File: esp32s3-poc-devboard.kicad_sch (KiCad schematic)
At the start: 69 parts, among them J1 24VDC, J2 Conn_01x01_Pin, J3 USB_C_Receptacle_USB2.0_14P, J4 USB_C_Receptacle_USB2.0_14P, Q3 MMDT5551, SW1 SW_Push, SW2 SW_Push, U1 ESP32-S3, U2 AMS1117-3.3, U3 XC6206P332MR, U4 TPS5430DDA, U5 CP2102N-A02-GQFN24, U6 USBLC6-2SC6, U7 USBLC6-2SC6

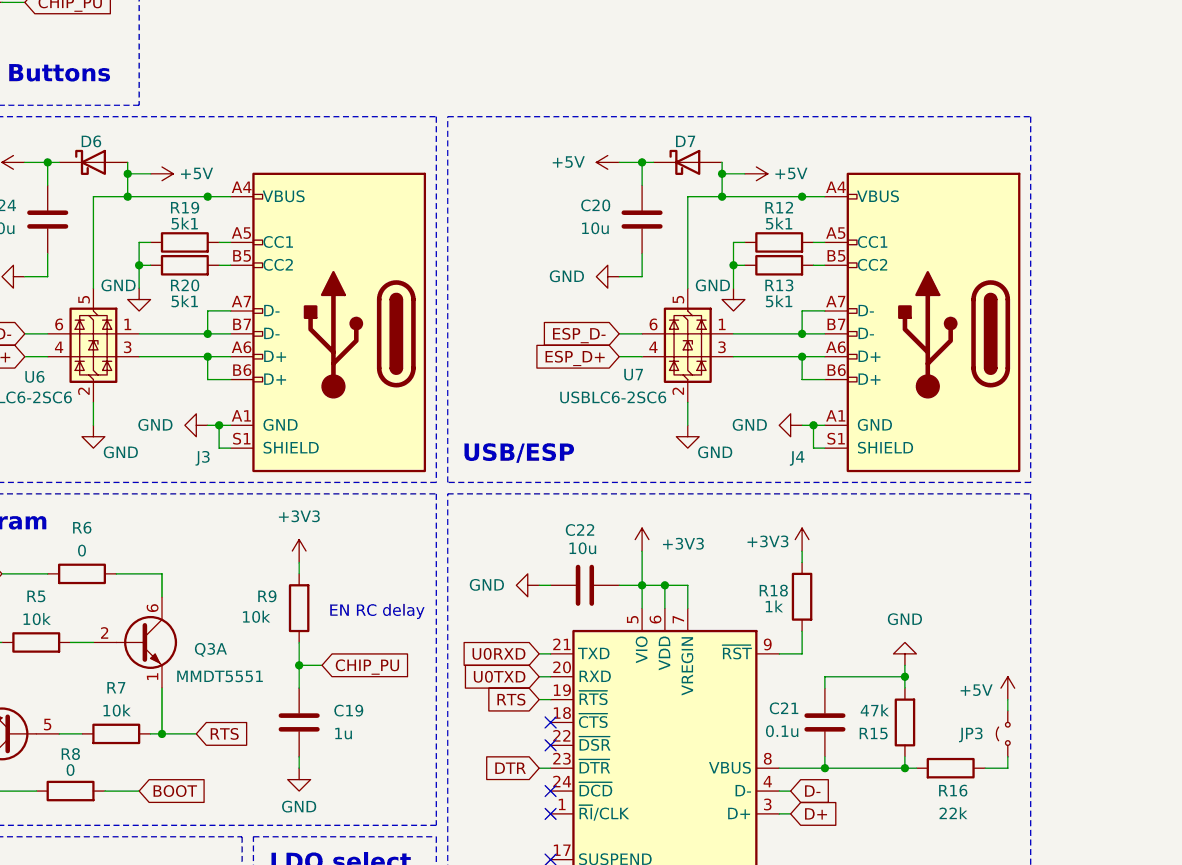
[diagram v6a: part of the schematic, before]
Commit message: add vbus to avoid feeding usb from smps
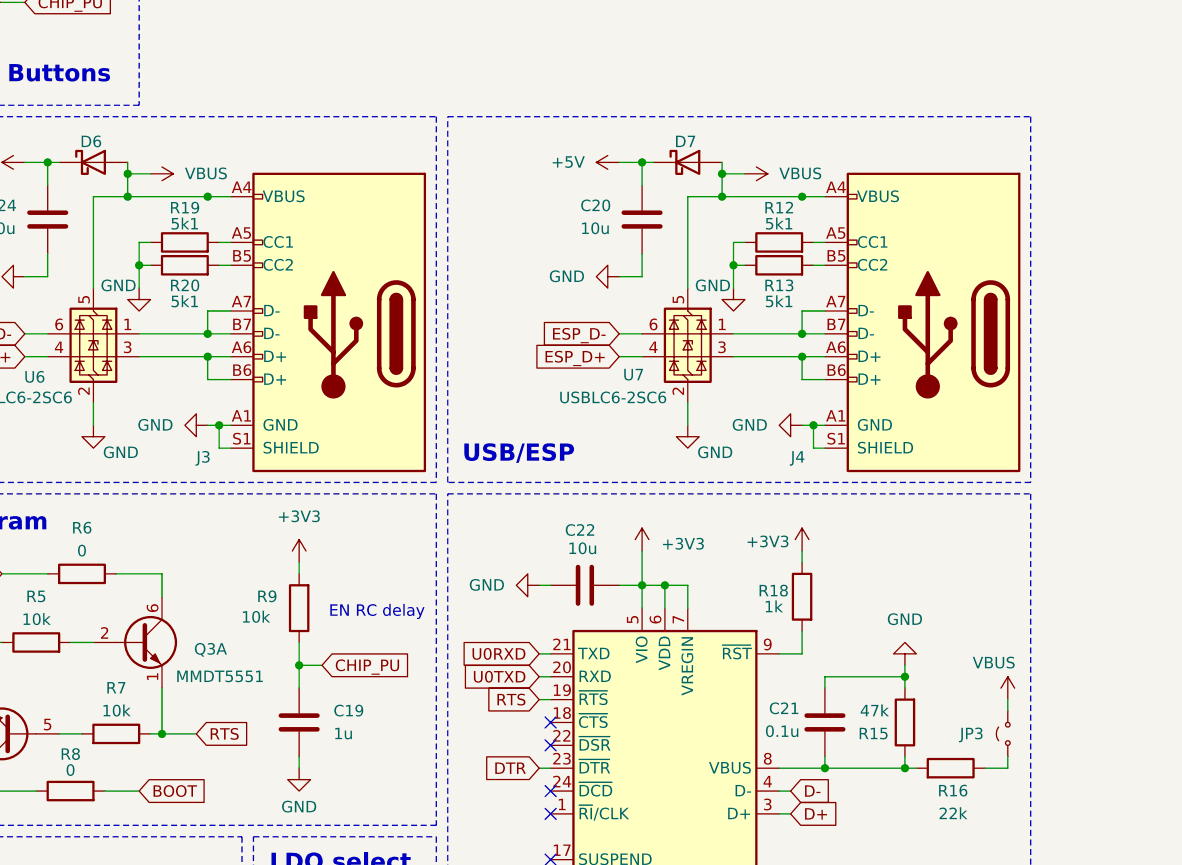
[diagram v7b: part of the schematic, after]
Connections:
- net +5V: no longer D6.2 (A), D7.2 (A), J3.A4 (VBUS), J3.A9 (VBUS), J3.B4 (VBUS), J3.B9 (VBUS), J4.A4 (VBUS), J4.A9 (VBUS), J4.B4 (VBUS), J4.B9 (VBUS), JP3.2 (B), U6.5 (VBUS), U7.5 (VBUS)
- new net VBUS: D6.2 (A), D7.2 (A), J3.A4 (VBUS), J3.A9 (VBUS), J3.B4 (VBUS), J3.B9 (VBUS), J4.A4 (VBUS), J4.A9 (VBUS), J4.B4 (VBUS), J4.B9 (VBUS), JP3.2 (B), U6.5 (VBUS), U7.5 (VBUS)
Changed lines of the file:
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@@
 	)
 	(symbol
-		(lib_id "power:+5V")
-		(at 116.84 45.72 270)
-		(mirror x)
-		(unit 1)
-		(exclude_from_sim no)
-		(in_bom yes)
-		(on_board yes)
-		(dnp no)
-		(property "Reference" "#PWR048"
-			(at 113.03 45.72 0)
-			(effects
-				(font
-					(size 1.27 1.27)
-				)
-				(hide yes)
-			)
-		)
-		(property "Value" "+5V"
-			(at 121.92 45.72 90)
-			(effects
-				(font
-					(size 1.27 1.27)
-				)
-			)
-		)
-		(property "Footprint" ""
-			(at 116.84 45.72 0)
-			(effects
-				(font
-					(size 1.27 1.27)
-				)
-				(hide yes)
-			)
-		)
-		(property "Datasheet" ""
-			(at 116.84 45.72 0)
-			(effects
-				(font
-					(size 1.27 1.27)
-				)
-				(hide yes)
-			)
-		)
-		(property "Description" "Power symbol creates a global label with name \"+5V\""
-			(at 116.84 45.72 0)
-			(effects
-				(font
-					(size 1.27 1.27)
-				)
-				(hide yes)
-			)
-		)
-		(pin "1"
-		)
-		(instances
-			(project "esp32s3-poc-devboard"
-				(path "/a6beb550-83d0-4746-bc61-cde76b7466a3"
-					(reference "#PWR048")
-					(unit 1)
-				)
-			)
-		)
-	)
-	(symbol
 		(lib_id "Device:R")
 		(at 69.85 140.97 180)
@@
 	)
 	(symbol
-		(lib_id "power:+5V")
-		(at 146.05 104.14 0)
-		(mirror y)
-		(unit 1)
-		(exclude_from_sim no)
-		(in_bom yes)
-		(on_board yes)
-		(dnp no)
-		(property "Reference" "#PWR037"
-			(at 146.05 107.95 0)
-			(effects
-				(font
-					(size 1.27 1.27)
-				)
-				(hide yes)
-			)
-		)
-		(property "Value" "+5V"
-			(at 142.494 103.124 0)
-			(effects
-				(font
-					(size 1.27 1.27)
-				)
-			)
-		)
-		(property "Footprint" ""
-			(at 146.05 104.14 0)
-			(effects
-				(font
-					(size 1.27 1.27)
-				)
-				(hide yes)
-			)
-		)
-		(property "Datasheet" ""
-			(at 146.05 104.14 0)
-			(effects
-				(font
-					(size 1.27 1.27)
-				)
-				(hide yes)
-			)
-		)
-		(property "Description" "Power symbol creates a global label with name \"+5V\""
-			(at 146.05 104.14 0)
-			(effects
-				(font
-					(size 1.27 1.27)
-				)
-				(hide yes)
-			)
-		)
-		(pin "1"
-		)
-		(instances
-			(project "esp32s3-poc-devboard"
-				(path "/a6beb550-83d0-4746-bc61-cde76b7466a3"
-					(reference "#PWR037")
-					(unit 1)
-				)
-			)
-		)
-	)
-	(symbol
 		(lib_id "power:GND")
 		(at 48.26 184.15 0)
@@
 	)
 	(symbol
-		(lib_id "power:+5V")
-		(at 50.8 45.72 270)
-		(mirror x)
-		(unit 1)
-		(exclude_from_sim no)
-		(in_bom yes)
-		(on_board yes)
-		(dnp no)
-		(property "Reference" "#PWR042"
-			(at 46.99 45.72 0)
-			(effects
-				(font
-					(size 1.27 1.27)
-				)
-				(hide yes)
-			)
-		)
-		(property "Value" "+5V"
-			(at 55.88 45.72 90)
-			(effects
-				(font
-					(size 1.27 1.27)
-				)
-			)
-		)
-		(property "Footprint" ""
-			(at 50.8 45.72 0)
-			(effects
-				(font
-					(size 1.27 1.27)
-				)
-				(hide yes)
-			)
-		)
-		(property "Datasheet" ""
-			(at 50.8 45.72 0)
-			(effects
-				(font
-					(size 1.27 1.27)
-				)
-				(hide yes)
-			)
-		)
-		(property "Description" "Power symbol creates a global label with name \"+5V\""
-			(at 50.8 45.72 0)
-			(effects
-				(font
-					(size 1.27 1.27)
-				)
-				(hide yes)
-			)
-		)
-		(pin "1"
-		)
-		(instances
-			(project "esp32s3-poc-devboard"
-				(path "/a6beb550-83d0-4746-bc61-cde76b7466a3"
-					(reference "#PWR042")
-					(unit 1)
-				)
-			)
-		)
-	)
-	(symbol
 		(lib_id "power:GND")
 		(at 153.67 182.88 0)
@@
 	)
 	(symbol
+		(lib_id "power:VBUS")
+		(at 50.8 45.72 270)
+		(unit 1)
+		(exclude_from_sim no)
+		(in_bom yes)
+		(on_board yes)
+		(dnp no)
+		(fields_autoplaced yes)
+		(property "Reference" "#PWR042"
+			(at 46.99 45.72 0)
+			(effects
+				(font
+					(size 1.27 1.27)
+				)
+				(hide yes)
+			)
+		)
+		(property "Value" "VBUS"
+			(at 54.61 45.7199 90)
+			(effects
+				(font
+					(size 1.27 1.27)
+				)
+				(justify left)
+			)
+		)
+		(property "Footprint" ""
+			(at 50.8 45.72 0)
+			(effects
+				(font
+					(size 1.27 1.27)
+				)
+				(hide yes)
+			)
+		)
+		(property "Datasheet" ""
+			(at 50.8 45.72 0)
+			(effects
+				(font
+					(size 1.27 1.27)
+				)
+				(hide yes)
+			)
+		)
+		(property "Description" "Power symbol creates a global label with name \"VBUS\""
+			(at 50.8 45.72 0)
+			(effects
+				(font
+					(size 1.27 1.27)
+				)
+				(hide yes)
+			)
+		)
+		(pin "1"
+		)
+		(instances
+			(project ""
+				(path "/a6beb550-83d0-4746-bc61-cde76b7466a3"
+					(reference "#PWR042")
+					(unit 1)
+				)
+			)
+		)
+	)
+	(symbol
 		(lib_id "power:+3V3")
 		(at 248.92 55.88 0)
@@
 	)
 	(symbol
+		(lib_id "power:VBUS")
+		(at 116.84 45.72 270)
+		(unit 1)
+		(exclude_from_sim no)
+		(in_bom yes)
+		(on_board yes)
+		(dnp no)
+		(fields_autoplaced yes)
+		(property "Reference" "#PWR051"
+			(at 113.03 45.72 0)
+			(effects
+				(font
+					(size 1.27 1.27)
+				)
+				(hide yes)
+			)
+		)
+		(property "Value" "VBUS"
+			(at 120.65 45.7199 90)
+			(effects
+				(font
+					(size 1.27 1.27)
+				)
+				(justify left)
+			)
+		)
+		(property "Footprint" ""
+			(at 116.84 45.72 0)
+			(effects
+				(font
+					(size 1.27 1.27)
+				)
+				(hide yes)
+			)
+		)
+		(property "Datasheet" ""
+			(at 116.84 45.72 0)
+			(effects
+				(font
+					(size 1.27 1.27)
+				)
+				(hide yes)
+			)
+		)
+		(property "Description" "Power symbol creates a global label with name \"VBUS\""
+			(at 116.84 45.72 0)
+			(effects
+				(font
+					(size 1.27 1.27)
+				)
+				(hide yes)
+			)
+		)
+		(pin "1"
+		)
+		(instances
+			(project ""
+				(path "/a6beb550-83d0-4746-bc61-cde76b7466a3"
+					(reference "#PWR051")
+					(unit 1)
+				)
+			)
+		)
+	)
+	(symbol
 		(lib_id "power:GND")
 		(at 72.39 125.73 90)
@@
 					(unit 1)
 				)
+			)
+		)
+	)
+	(symbol
+		(lib_id "power:VBUS")
+		(at 146.05 104.14 0)
+		(unit 1)
+		(exclude_from_sim no)
+		(in_bom yes)
+		(on_board yes)
+		(dnp no)
+		(property "Reference" "#PWR048"
+			(at 146.05 107.95 0)
+			(effects
+				(font
+					(size 1.27 1.27)
+				)
+				(hide yes)
+			)
+		)
+		(property "Value" "VBUS"
+			(at 144.526 100.076 0)
+			(effects
+				(font
+					(size 1.27 1.27)
+				)
+			)
+		)
+		(property "Footprint" ""
+			(at 146.05 104.14 0)
+			(effects
+				(font
+					(size 1.27 1.27)
+				)
+				(hide yes)
+			)
+		)
+		(property "Datasheet" ""
+			(at 146.05 104.14 0)
+			(effects
+				(font
+					(size 1.27 1.27)
+				)
+				(hide yes)
+			)
+		)
+		(property "Description" "Power symbol creates a global label with name \"VBUS\""
+			(at 146.05 104.14 0)
+			(effects
+				(font
+					(size 1.27 1.27)
+				)
+				(hide yes)
+			)
+		)
+		(pin "1"
+		)
+		(instances
+			(project ""
+				(path "/a6beb550-83d0-4746-bc61-cde76b7466a3"
+					(reference "#PWR048")
+					(unit 1)
+				)
